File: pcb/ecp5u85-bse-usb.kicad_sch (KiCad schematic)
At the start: 23 parts, among them J1 BSE-040-01-X-D-A, J2 BSE-040-01-X-D-A

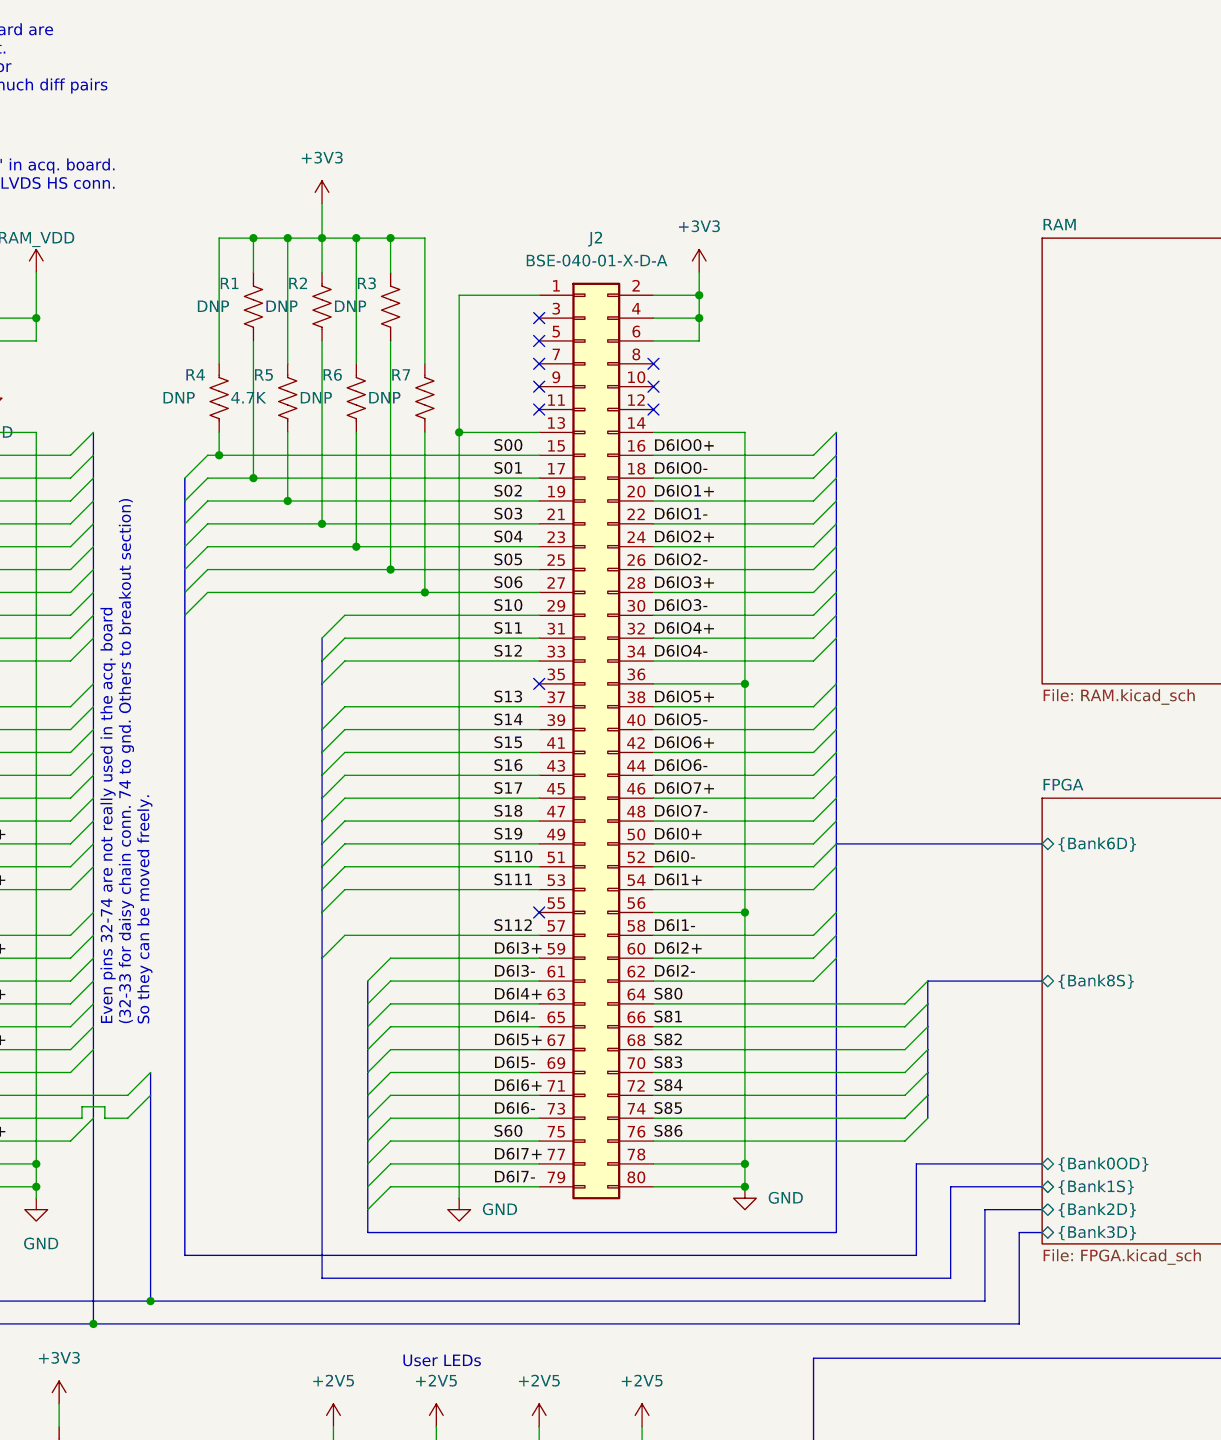
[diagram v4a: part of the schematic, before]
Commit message: Rearrange SAMTEC buses
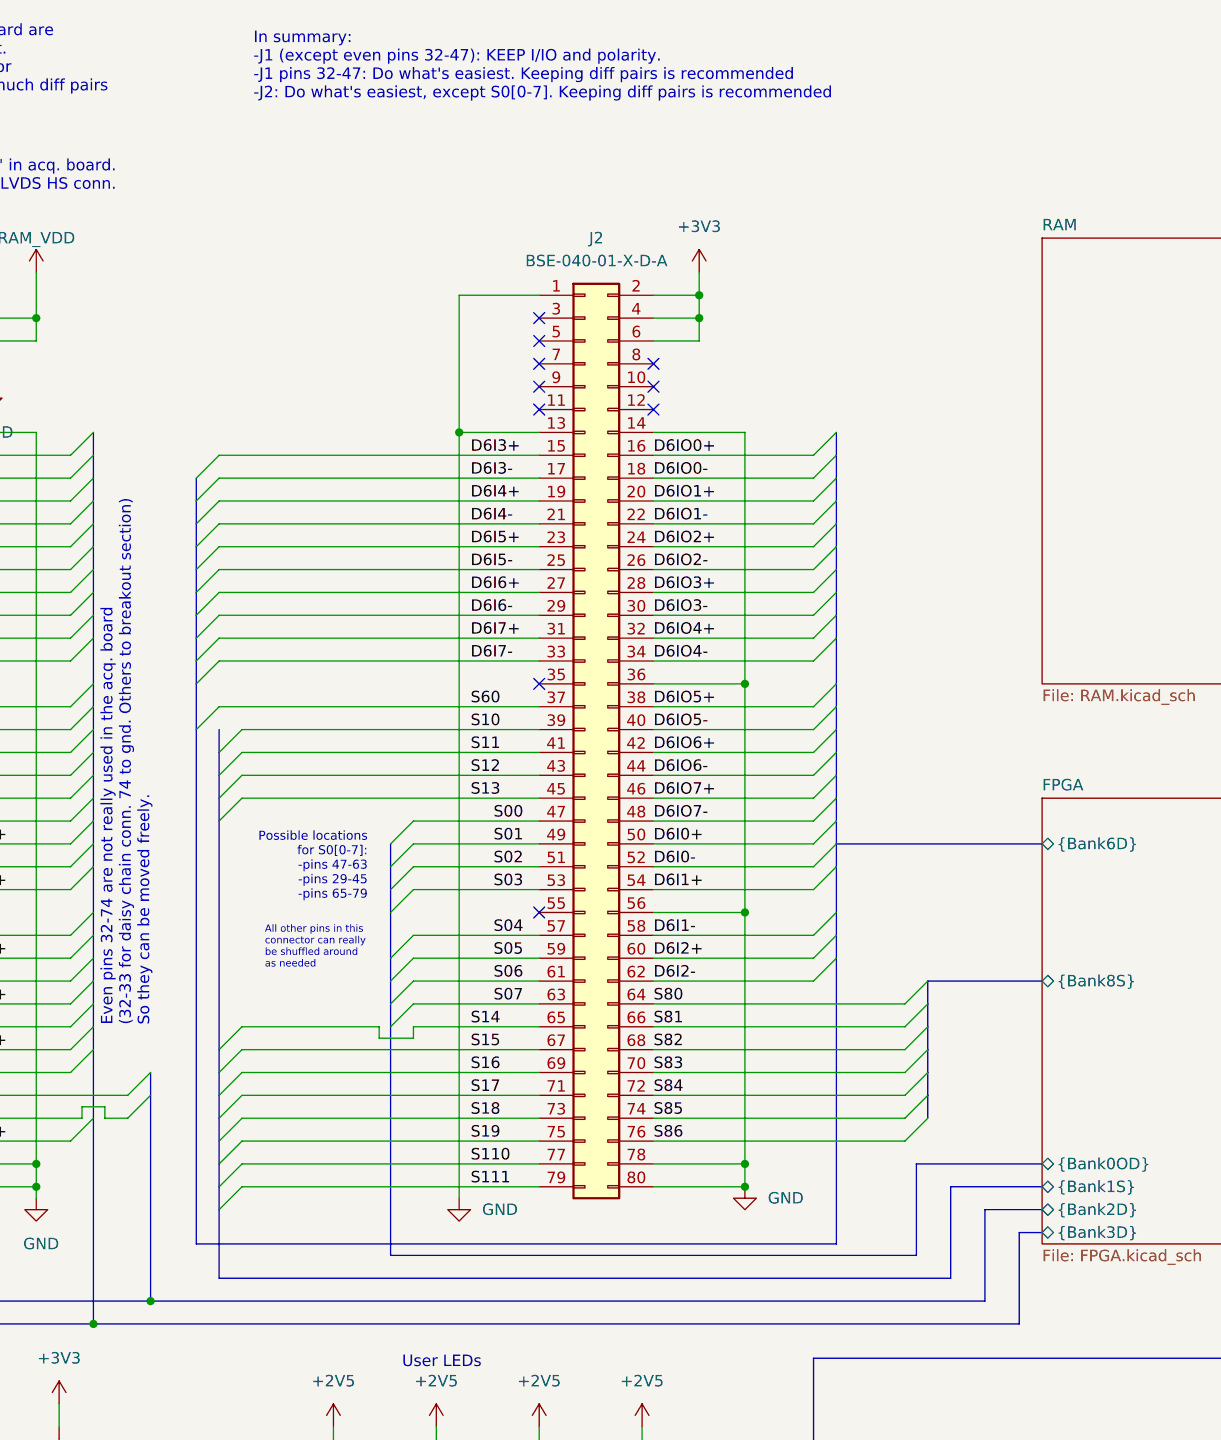
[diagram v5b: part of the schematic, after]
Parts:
- removed R1, R2, R3, R4, R6, R7: DNP, Resistor_SMD:R_0402_1005Metric, symbol Device:R_US
- removed R5: 4.7K, Resistor_SMD:R_0402_1005Metric, symbol Device:R_US
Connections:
- net S112 is gone; now on net S04: J2.57 (Pin_57)
- net D6I3+: now also J2.15 (Pin_15); no longer J2.59 (Pin_59)
- net D6I3-: now also J2.17 (Pin_17); no longer J2.61 (Pin_61)
- net D6I4+: now also J2.19 (Pin_19); no longer J2.63 (Pin_63)
- net D6I4-: now also J2.21 (Pin_21); no longer J2.65 (Pin_65)
- net D6I5+: now also J2.23 (Pin_23); no longer J2.67 (Pin_67)
- net D6I5-: now also J2.25 (Pin_25); no longer J2.69 (Pin_69)
- net D6I6+: now also J2.27 (Pin_27); no longer J2.71 (Pin_71)
- net D6I6-: now also J2.29 (Pin_29); no longer J2.73 (Pin_73)
- net D6I7+: now also J2.31 (Pin_31); no longer J2.77 (Pin_77)
- net D6I7-: now also J2.33 (Pin_33); no longer J2.79 (Pin_79)
- net S00: now also J2.47 (Pin_47); no longer J2.15 (Pin_15)
- net S01: now also J2.49 (Pin_49); no longer J2.17 (Pin_17)
- net S02: now also J2.51 (Pin_51); no longer J2.19 (Pin_19)
- net S03: now also J2.53 (Pin_53); no longer J2.21 (Pin_21)
- net S04: no longer J2.23 (Pin_23)
- net S05: now also J2.59 (Pin_59); no longer J2.25 (Pin_25)
- net S06: now also J2.61 (Pin_61); no longer J2.27 (Pin_27)
- net S10: now also J2.39 (Pin_39); no longer J2.29 (Pin_29)
- net S11: now also J2.41 (Pin_41); no longer J2.31 (Pin_31)
- net S110: now also J2.77 (Pin_77); no longer J2.51 (Pin_51)
- net S111: now also J2.79 (Pin_79); no longer J2.53 (Pin_53)
- net S12: now also J2.43 (Pin_43); no longer J2.33 (Pin_33)
- net S13: now also J2.45 (Pin_45); no longer J2.37 (Pin_37)
- net S14: now also J2.65 (Pin_65); no longer J2.39 (Pin_39)
- net S15: now also J2.67 (Pin_67); no longer J2.41 (Pin_41)
- net S16: now also J2.69 (Pin_69); no longer J2.43 (Pin_43)
- net S17: now also J2.71 (Pin_71); no longer J2.45 (Pin_45)
- net S18: now also J2.73 (Pin_73); no longer J2.47 (Pin_47)
- net S19: now also J2.75 (Pin_75); no longer J2.49 (Pin_49)
- net S60: now also J2.37 (Pin_37); no longer J2.75 (Pin_75)
- new net S07: J2.63 (Pin_63)
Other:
- note added: "All other pins in this connector can really be shuffled around as needed"
- note added: "In summary: -J1 (except even pins 32-47): KEEP I/IO and polarity. -J1 pins 32-47: Do what's easiest. Keeping diff pairs is recommended -J2: Do what's easiest, except S0[0-7]. Keeping diff pairs is recommended"
- note added: "Possible locations for S0[0-7]: -pins 47-63 -pins 29-45 -pins 65-79"

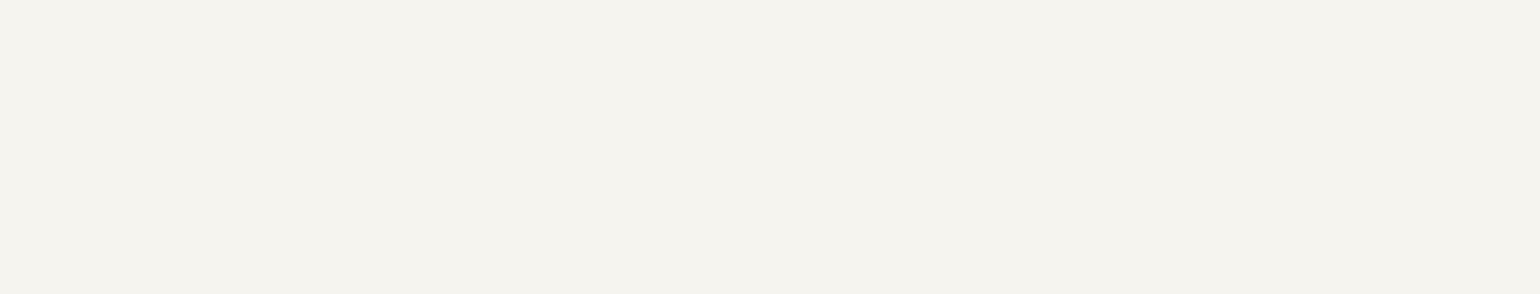
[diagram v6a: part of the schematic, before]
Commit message: FPGA is broken out
- Side connectors will need some pin swaps
- The RAM and FTDI buses need to be retuned because they got moved
around during this process
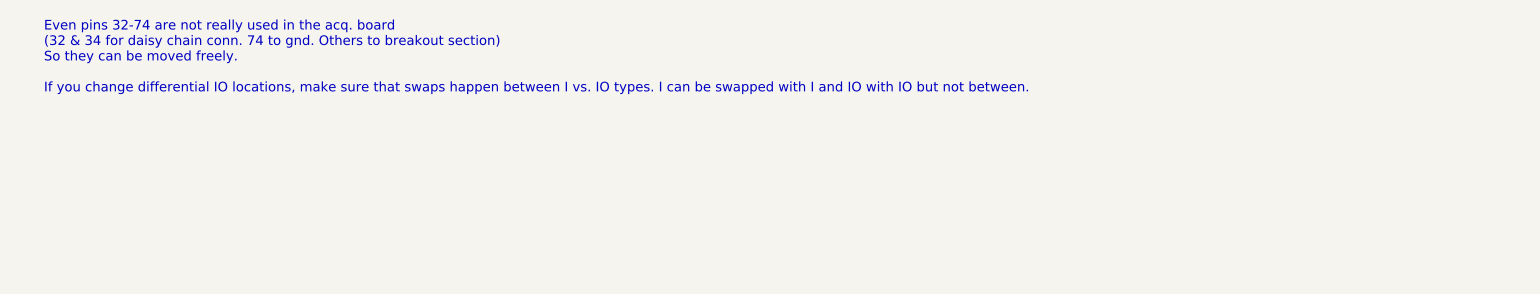
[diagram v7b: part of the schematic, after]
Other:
- note added: "Even pins 32-74 are not really used in the acq. board (32 & 34 for daisy chain conn. 74 to gnd. Others to breakout section) So they can be moved freely. If you change differential IO locations, make sure that swaps happen between I vs. IO types. I can be swapped with I and IO with IO but not between."
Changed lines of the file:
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@@
+    (effects (font (size 1.27 1.27)) (justify left bottom))
+  )
+  (text "Even pins 32-74 are not really used in the acq. board\n(32 & 34 for daisy chain conn. 74 to gnd. Others to breakout section)\nSo they can be moved freely. \n\nIf you change differential IO locations, make sure that swaps happen between I vs. IO types. I can be swapped with I and IO with IO but not between."
+    (at 17.78 -15.24 0)
     (effects (font (size 1.27 1.27)) (justify left bottom))
   )
@@
       (reference "C1") (unit 1) (value "100n") (footprint "Capacitor_SMD:C_0402_1005Metric")
     )
-    (path "/b14c35da-dd14-4b8d-93a9-00f219a92f41/f5708ce6-44be-4a9d-a945-68ba4d9a2b18"
-      (reference "C2") (unit 1) (value "1u") (footprint "Capacitor_SMD:C_0603_1608Metric")
-    )
-    (path "/b14c35da-dd14-4b8d-93a9-00f219a92f41/087d99fd-f9ef-4815-af7f-587c0104acbf"
-      (reference "C3") (unit 1) (value "10u") (footprint "Capacitor_SMD:C_0805_2012Metric")
-    )
     (path "/b14c35da-dd14-4b8d-93a9-00f219a92f41/318ccd14-3fc7-4585-99cf-7409bc51fcc3"
